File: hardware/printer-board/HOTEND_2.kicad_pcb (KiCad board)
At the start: 2 copper layers, 7 parts, among them J25 HOT_END, Q4 WSK220N04

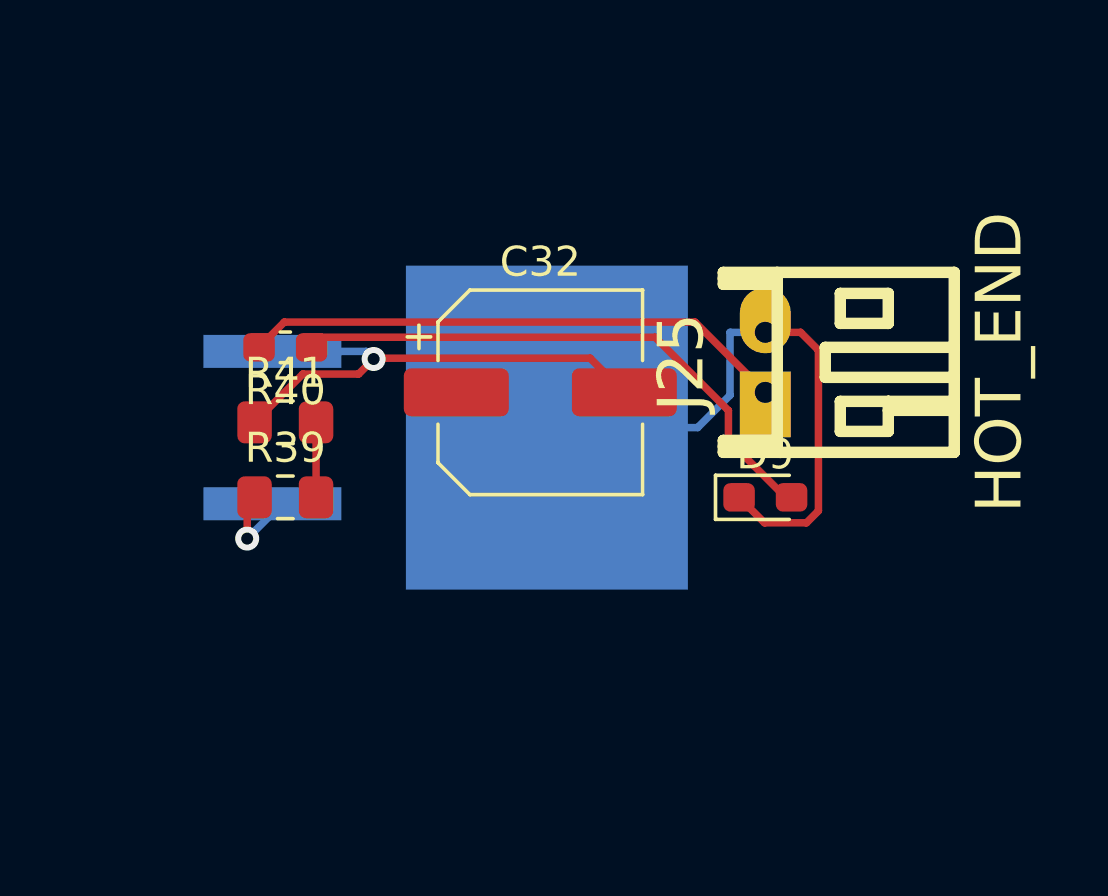
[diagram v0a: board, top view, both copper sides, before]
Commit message: update hotend,
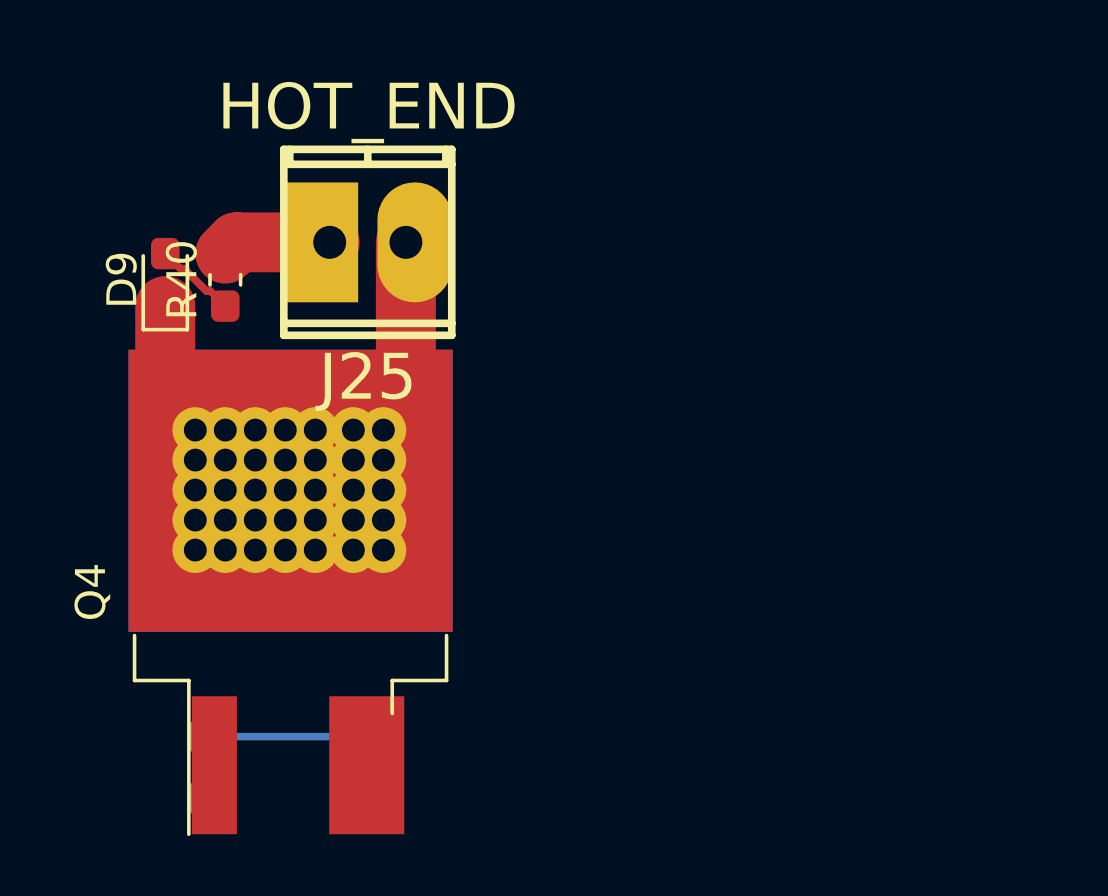
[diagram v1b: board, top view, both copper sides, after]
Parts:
- removed C32: CP100uf,16V, Capacitor_SMD:CP_Elec_6.3x5.3
- J25: footprint footprint-lib:s2b-ph-kl,hotend_output -> footprint-lib:mpt_0,5%2f2-2,54,heatbed
- Q4: footprint Package_TO_SOT_SMD:TO-263-2 -> footprint-lib:TO-263-2,drill_array; moved to F.Cu
- R39, R41: moved to B.Cu
- moved D9 21.3 mm to (4.00, 8.25), turned to 90 degrees
- moved J25 13.8 mm to (10.8, 7.00), turned to 180 degrees
- moved R41 11.8 mm to (10.8, 24.5), turned to 90 degrees
- moved R39 9.34 mm to (5.50, 24.5), turned to 90 degrees
- moved Q4 7.53 mm to (8.18, 18.7), turned to 90 degrees
- moved R40 3.01 mm to (6.00, 8.25), turned to 90 degrees
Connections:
- net Net-(D9-Pad1) renamed /-12V
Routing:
- net GND: track 17.2 -> 0.00 mm, vias 1 -> 0
- net Net-(D9-Pad2): track 18.9 -> 2.72 mm
- net +12V: track 18.2 -> 3.64 mm
- net Net-(Q4-Pad1): track 2.98 -> 0.00 mm, vias 1 -> 0
- net /HOTEND_EN: track 2.50 -> 5.25 mm
- net /-12V: track 20.4 -> 18.1 mm
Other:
- net class +12V_HC added: clearance 0.2, trace_width 2, via_dia 0.8, via_drill 0.4
- net class GND added: clearance 0.2, trace_width 2, via_dia 0.8, via_drill 0.4

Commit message: update for stepper Z,
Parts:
- added C1: CP100uf,35V, Capacitor_SMD:C_0603_1608Metric_Pad1.05x0.95mm_HandSolder, F.Cu at (190.6, 45.3)
- added C10: CP100uf,25V, Capacitor_SMD:CP_Elec_6.3x7.7, F.Cu at (297.3, 53.2)
- added C11: C104,0603, Capacitor_SMD:C_0603_1608Metric_Pad1.05x0.95mm_HandSolder, F.Cu at (297.6, 59.1)
- added C12: CP100uf,25V, Capacitor_SMD:CP_Elec_6.3x7.7, F.Cu at (240.3, 109.1)
- added C13: C104,0603, Capacitor_SMD:C_0603_1608Metric_Pad1.05x0.95mm_HandSolder, F.Cu at (237.3, 115.0)
- added C14: C106,0603, Capacitor_SMD:C_0603_1608Metric_Pad1.05x0.95mm_HandSolder, F.Cu at (295.6, 127.7)
- added C15: C106,0603, Capacitor_SMD:C_0603_1608Metric_Pad1.05x0.95mm_HandSolder, F.Cu at (292.3, 136.8)
- added C16: C106,0603, Capacitor_SMD:C_0603_1608Metric_Pad1.05x0.95mm_HandSolder, F.Cu at (292.3, 127.7)
- added C17: C106,0603, Capacitor_SMD:C_0603_1608Metric_Pad1.05x0.95mm_HandSolder, F.Cu at (295.6, 129.2)
- added C18: C106,0603, Capacitor_SMD:C_0603_1608Metric_Pad1.05x0.95mm_HandSolder, F.Cu at (292.3, 132.3)
- added C19: C104,0603, Capacitor_SMD:C_0603_1608Metric_Pad1.05x0.95mm_HandSolder, F.Cu at (221.4, 140.3)
- added C2: CP100uf,25V, Capacitor_SMD:CP_Elec_6.3x7.7, F.Cu at (160.0, 109.1)
- added C20: CP100uf,35V, Capacitor_SMD:CP_Elec_6.3x7.7, F.Cu at (235.1, 137.6)
- added C21: C104,0603, Capacitor_SMD:C_0603_1608Metric_Pad1.05x0.95mm_HandSolder, F.Cu at (295.3, 86.0)
- added C22: C10pf,0603, Capacitor_SMD:C_0603_1608Metric_Pad1.05x0.95mm_HandSolder, F.Cu at (281.9, 85.8)
- added C23: C104,0603, Capacitor_SMD:C_0603_1608Metric_Pad1.05x0.95mm_HandSolder, F.Cu at (308.3, 76.8)
- added C24: C10pf,0603, Capacitor_SMD:C_0603_1608Metric_Pad1.05x0.95mm_HandSolder, F.Cu at (285.2, 85.8)
- added C25: C104,0603, Capacitor_SMD:C_0603_1608Metric_Pad1.05x0.95mm_HandSolder, F.Cu at (295.1, 82.0)
- added C26: C104,0603, Capacitor_SMD:C_0603_1608Metric_Pad1.05x0.95mm_HandSolder, F.Cu at (295.1, 80.4)
- added C27: C104,0603, Capacitor_SMD:C_0603_1608Metric_Pad1.05x0.95mm_HandSolder, F.Cu at (298.5, 80.4)
- added C28: C104,0603, Capacitor_SMD:C_0603_1608Metric_Pad1.05x0.95mm_HandSolder, F.Cu at (295.1, 83.5)
- added C29: C105,0603, Capacitor_SMD:C_0603_1608Metric_Pad1.05x0.95mm_HandSolder, F.Cu at (305.0, 75.3)
- added C3: C104,0603, Capacitor_SMD:C_0603_1608Metric_Pad1.05x0.95mm_HandSolder, F.Cu at (166.4, 109.9)
- added C30: C104,0603, Capacitor_SMD:C_0603_1608Metric_Pad1.05x0.95mm_HandSolder, F.Cu at (298.5, 78.9)
- added C31: C104,0603, Capacitor_SMD:C_0603_1608Metric_Pad1.05x0.95mm_HandSolder, F.Cu at (291.9, 85.8)
- added C32: C104,0603, Capacitor_SMD:C_0603_1608Metric_Pad1.05x0.95mm_HandSolder, F.Cu at (288.6, 85.8)
- added C33: CP220uf,16V, Capacitor_SMD:C_0603_1608Metric_Pad1.05x0.95mm_HandSolder, F.Cu at (147.7, 149.0)
- added C34: CP220uf,16V, Capacitor_SMD:C_0603_1608Metric_Pad1.05x0.95mm_HandSolder, F.Cu at (144.3, 149.0)
- added C35: CP220uf,25V, Capacitor_SMD:C_0603_1608Metric_Pad1.05x0.95mm_HandSolder, F.Cu at (144.3, 150.5)
- added C36: CP100uf,16V, Capacitor_SMD:CP_Elec_6.3x5.3, F.Cu at (259.2, 130.5)
- added C37: CP100uf,16V, Capacitor_SMD:CP_Elec_6.3x5.3, F.Cu at (321.8, 48.1)
- added C38: CP100uf,16V, Capacitor_SMD:CP_Elec_6.3x5.3, F.Cu at (259.2, 145.1)
- added C39: CP100uf,25V, Capacitor_SMD:CP_Elec_6.3x7.7, F.Cu at (257.2, 77.0)
- added C4: CP100uf,25V, Capacitor_SMD:CP_Elec_6.3x7.7, F.Cu at (200.2, 109.1)
- added C40: C104,0603, Capacitor_SMD:C_0603_1608Metric_Pad1.05x0.95mm_HandSolder, F.Cu at (254.2, 84.5)
- added C41: CP100uf,25V, Capacitor_SMD:CP_Elec_6.3x7.7, F.Cu at (257.2, 53.2)
- added C42: C104,0603, Capacitor_SMD:C_0603_1608Metric_Pad1.05x0.95mm_HandSolder, F.Cu at (263.6, 54.0)
- added C43: C104,0603, Capacitor_SMD:C_0603_1608Metric_Pad1.05x0.95mm_HandSolder, F.Cu at (274.0, 103.0)
- added C44: CP100uf,16V, Capacitor_SMD:CP_Elec_6.3x5.3, F.Cu at (280.3, 95.8)
- added C45: C106,0603, Capacitor_SMD:C_0603_1608Metric_Pad1.05x0.95mm_HandSolder, F.Cu at (318.6, 92.3)
- added C46: C104,0603, Capacitor_SMD:C_0603_1608Metric_Pad1.05x0.95mm_HandSolder, F.Cu at (325.3, 92.3)
- added C47: C332,0603, Capacitor_SMD:C_0603_1608Metric_Pad1.05x0.95mm_HandSolder, F.Cu at (322.0, 92.3)
- added C48: C103,0603, Capacitor_SMD:C_0603_1608Metric_Pad1.05x0.95mm_HandSolder, F.Cu at (318.6, 93.8)
- added C49: C226,6.3v,0603, Capacitor_SMD:C_0603_1608Metric_Pad1.05x0.95mm_HandSolder, F.Cu at (328.7, 93.8)
- added C5: C104,0603, Capacitor_SMD:C_0603_1608Metric_Pad1.05x0.95mm_HandSolder, F.Cu at (197.2, 116.6)
- added C50: C106,0603, Capacitor_SMD:C_0603_1608Metric_Pad1.05x0.95mm_HandSolder, F.Cu at (224.8, 152.9)
- added C51: C104,0603, Capacitor_SMD:C_0603_1608Metric_Pad1.05x0.95mm_HandSolder, F.Cu at (228.1, 151.4)
- added C52: C332,0603, Capacitor_SMD:C_0603_1608Metric_Pad1.05x0.95mm_HandSolder, F.Cu at (221.4, 152.9)
- added C53: C103,0603, Capacitor_SMD:C_0603_1608Metric_Pad1.05x0.95mm_HandSolder, F.Cu at (224.8, 151.4)
- added C54: C226,6.3v,0603, Capacitor_SMD:C_0603_1608Metric_Pad1.05x0.95mm_HandSolder, F.Cu at (221.4, 151.4)
- added C6: CP100uf,25V, Capacitor_SMD:CP_Elec_6.3x7.7, F.Cu at (160.0, 133.1)
- added C7: C104,0603, Capacitor_SMD:C_0603_1608Metric_Pad1.05x0.95mm_HandSolder, F.Cu at (160.3, 139.0)
- added C8: CP100uf,25V, Capacitor_SMD:CP_Elec_6.3x7.7, F.Cu at (200.1, 133.1)
- added C9: C104,0603, Capacitor_SMD:C_0603_1608Metric_Pad1.05x0.95mm_HandSolder, F.Cu at (197.1, 140.5)
- added D1: 5V HEALTHY, LED_SMD:LED_0603_1608Metric_Pad1.05x0.95mm_HandSolder, F.Cu at (141.2, 93.6)
- added D10: LED_BLUE,0603, LED_SMD:LED_0603_1608Metric_Pad1.05x0.95mm_HandSolder, F.Cu at (315.2, 79.3)
- added D11: LED_BLUE,0603, LED_SMD:LED_0603_1608Metric_Pad1.05x0.95mm_HandSolder, F.Cu at (318.6, 79.3)
- added D12: LED_BLUE,0603, LED_SMD:LED_0603_1608Metric_Pad1.05x0.95mm_HandSolder, F.Cu at (318.6, 80.9)
- added D13: LED_BLUE,0603, LED_SMD:LED_0603_1608Metric_Pad1.05x0.95mm_HandSolder, F.Cu at (325.4, 79.3)
- added D14: LED_BLUE,0603, LED_SMD:LED_0603_1608Metric_Pad1.05x0.95mm_HandSolder, F.Cu at (322.0, 79.3)
- added D15: SD_M4, Diode_SMD:D_SOD-323_HandSoldering, F.Cu at (221.8, 136.1)
- added D16: SD_M4, Diode_SMD:D_SOD-323_HandSoldering, F.Cu at (225.8, 136.1)
- added D17: PB9, LED_SMD:LED_0603_1608Metric_Pad1.05x0.95mm_HandSolder, F.Cu at (278.5, 85.8)
- added D18: LED_RED,0603, LED_SMD:LED_0603_1608Metric_Pad1.05x0.95mm_HandSolder, F.Cu at (295.3, 102.5)
- added D19: LED_RED,0603, LED_SMD:LED_0603_1608Metric_Pad1.05x0.95mm_HandSolder, F.Cu at (265.4, 122.5)
- added D2: LED_BLUE,0603, LED_SMD:LED_0603_1608Metric_Pad1.05x0.95mm_HandSolder, F.Cu at (157.0, 115.4)
- added D20: LED_BLUE,0603, LED_SMD:LED_0603_1608Metric_Pad1.05x0.95mm_HandSolder, F.Cu at (259.8, 134.9)
- added D21: LED_BLUE,0603, LED_SMD:LED_0603_1608Metric_Pad1.05x0.95mm_HandSolder, F.Cu at (322.4, 52.4)
- added D22: LED_BLUE,0603, LED_SMD:LED_0603_1608Metric_Pad1.05x0.95mm_HandSolder, F.Cu at (272.1, 142.3)
- added D23: LED_BLUE,0603, LED_SMD:LED_0603_1608Metric_Pad1.05x0.95mm_HandSolder, F.Cu at (254.2, 81.4)
- added D24: LED_BLUE,0603, LED_SMD:LED_0603_1608Metric_Pad1.05x0.95mm_HandSolder, F.Cu at (254.2, 57.5)
- added D3: LED_BLUE,0603, LED_SMD:LED_0603_1608Metric_Pad1.05x0.95mm_HandSolder, F.Cu at (197.2, 113.5)
- added D4: LED_BLUE,0603, LED_SMD:LED_0603_1608Metric_Pad1.05x0.95mm_HandSolder, F.Cu at (157.0, 137.4)
- added D5: LED_BLUE,0603, LED_SMD:LED_0603_1608Metric_Pad1.05x0.95mm_HandSolder, F.Cu at (197.1, 137.4)
- added D6: LED_BLUE,0603, LED_SMD:LED_0603_1608Metric_Pad1.05x0.95mm_HandSolder, F.Cu at (294.3, 57.5)
- added D7: LED_BLUE,0603, LED_SMD:LED_0603_1608Metric_Pad1.05x0.95mm_HandSolder, F.Cu at (237.3, 113.5)
- added D8: LED_RED,0603, LED_SMD:LED_0603_1608Metric_Pad1.05x0.95mm_HandSolder, F.Cu at (295.3, 119.1)
- added F1: 16V/30A, w_misc_comp:fuse_smf, F.Cu at (225.0, 127.0)
- added F2: 30V/5A, w_misc_comp:fuse_smf, F.Cu at (225.0, 132.4)
- added H1: MOUNT_M3, MountingHole:MountingHole_2.7mm_M2.5, F.Cu at (3.00, 3.00)
- added H2: MOUNT_M3, MountingHole:MountingHole_2.7mm_M2.5, F.Cu at (97.0, 3.00)
- added H3: MOUNT_M3, MountingHole:MountingHole_2.7mm_M2.5, F.Cu at (3.00, 97.0)
- added H4: MOUNT_M3, MountingHole:MountingHole_2.7mm_M2.5, F.Cu at (97.0, 97.0)
- added J1: USB_DEBUG, Connector_PinHeader_1.27mm:PinHeader_1x05_P1.27mm_Vertical, F.Cu at (187.4, 45.7)
- added J10: MS_SELECT, Connector_PinHeader_2.54mm:PinHeader_2x03_P2.54mm_Vertical, F.Cu at (304.8, 46.3)
- added J11: E0, footprint-lib:b4b-ph-kl,stepper_terminal, F.Cu at (297.8, 46.6)
- added J12: MS_SELECT, Connector_PinHeader_2.54mm:PinHeader_2x03_P2.54mm_Vertical, F.Cu at (247.8, 102.3)
- added J13: E1, footprint-lib:b4b-ph-kl,stepper_terminal, F.Cu at (240.8, 102.6)
- added J14: HEATBED, footprint-lib:mpt_0,5%2f2-2,54,heatbed, F.Cu at (309.5, 113.4)
- added J15: X_MIN, footprint-lib:b3b-ph-kl,end_stop, F.Cu at (317.7, 70.5)
- added J16: X_MAX, footprint-lib:b3b-ph-kl,end_stop, F.Cu at (317.7, 75.6)
- added J17: Y_MIN, footprint-lib:b3b-ph-kl,end_stop, F.Cu at (326.1, 70.5)
- added J18: Y_MAX, footprint-lib:b3b-ph-kl,end_stop, F.Cu at (326.1, 75.6)
- added J19: Z_MIN, footprint-lib:b3b-ph-kl,end_stop, F.Cu at (334.5, 70.5)
- added J2: MS_SELECT, Connector_PinHeader_2.54mm:PinHeader_2x03_P2.54mm_Vertical, F.Cu at (167.5, 102.3)
- added J20: Z_MAX, footprint-lib:b3b-ph-kl,end_stop, F.Cu at (334.5, 75.6)
- added J21: HEATBED_TEMP, w_conn_jst-ph:b2b-ph-kl, F.Cu at (281.1, 134.1)
- added J22: HOTEND_TEMP0, w_conn_jst-ph:b2b-ph-kl, F.Cu at (281.1, 129.1)
- added J23: HOTEND_TEMP1, w_conn_jst-ph:b2b-ph-kl, F.Cu at (287.4, 129.1)
- added J24: AUX_TEMP, w_conn_jst-ph:b2b-ph-kl, F.Cu at (287.4, 134.1)
- added J26: 12V_INPUT, footprint-lib:mpt_0,5%2f2-2,54,12V_SRC, F.Cu at (239.3, 130.8)
- added J27: 12V_OUT, footprint-lib:mpt_0,5%2f2-2,54,12V_SRC, F.Cu at (233.3, 130.8)
- added J28: SWD, Connector_PinHeader_1.27mm:PinHeader_1x04_P1.27mm_Vertical, F.Cu at (307.2, 69.6)
- added J29: USB_DEBUG, Connector_PinHeader_1.27mm:PinHeader_1x05_P1.27mm_Vertical, F.Cu at (157.4, 149.5)
- added J3: X, footprint-lib:b4b-ph-kl,stepper_terminal, F.Cu at (160.5, 102.6)
- added J30: PWR_DEBUG, Connector_PinHeader_1.27mm:PinHeader_1x05_P1.27mm_Vertical, F.Cu at (141.1, 149.5)
- added J31: HOT_END, footprint-lib:mpt_0,5%2f2-2,54,heatbed, F.Cu at (309.5, 96.8)
- added J32: HOT_END, footprint-lib:mpt_0,5%2f2-2,54,heatbed, F.Cu at (279.6, 116.8)
- added J33: TO FAN0, footprint-lib:b2b-ph-kl,fan_pwm_out, F.Cu at (267.2, 129.1)
- added J34: TO FAN1, footprint-lib:b2b-ph-kl,fan_pwm_out, F.Cu at (329.8, 46.6)
- added J35: TO FAN2, footprint-lib:b2b-ph-kl,fan_pwm_out, F.Cu at (267.2, 143.6)
- added J36: MS_SELECT, Connector_PinHeader_2.54mm:PinHeader_2x03_P2.54mm_Vertical, F.Cu at (264.7, 70.2)
- added J37: Z2, footprint-lib:b4b-ph-kl,stepper_terminal, F.Cu at (257.7, 70.5)
- added J38: MS_SELECT, Connector_PinHeader_2.54mm:PinHeader_2x03_P2.54mm_Vertical, F.Cu at (264.7, 46.3)
- added J39: Y, footprint-lib:b4b-ph-kl,stepper_terminal, F.Cu at (257.7, 46.6)
- added J4: MS_SELECT, Connector_PinHeader_2.54mm:PinHeader_2x03_P2.54mm_Vertical, F.Cu at (207.7, 102.3)
- added J40: Conn_01x07, Connector_PinHeader_1.27mm:PinHeader_1x07_P1.27mm_Vertical, F.Cu at (273.9, 93.4)
- added J41: EXP1, Connector_PinHeader_2.54mm:PinHeader_2x05_P2.54mm_Vertical, F.Cu at (261.8, 94.1)
- added J42: EXP2, Connector_PinHeader_2.54mm:PinHeader_2x05_P2.54mm_Vertical, F.Cu at (268.0, 94.1)
- added J5: Z, footprint-lib:b4b-ph-kl,stepper_terminal, F.Cu at (200.7, 102.6)
- added J6: MS_SELECT, Connector_PinHeader_2.54mm:PinHeader_2x03_P2.54mm_Vertical, F.Cu at (167.5, 126.2)
- added J7: Z1, footprint-lib:b4b-ph-kl,stepper_terminal, F.Cu at (160.5, 126.5)
- added J8: MS_SELECT, Connector_PinHeader_2.54mm:PinHeader_2x03_P2.54mm_Vertical, F.Cu at (207.6, 126.2)
- added J9: Z3, footprint-lib:b4b-ph-kl,stepper_terminal, F.Cu at (200.6, 126.5)
- added JP1: Jumper_NO_Small, Jumper:SolderJumper-2_P1.3mm_Open_TrianglePad1.0x1.5mm, F.Cu at (141.2, 95.7)
- added JP2: Jumper_NO_Small, Jumper:SolderJumper-2_P1.3mm_Open_TrianglePad1.0x1.5mm, F.Cu at (187.5, 54.7)
- added JP3: Jumper_NO_Small, Jumper:SolderJumper-2_P1.3mm_Open_TrianglePad1.0x1.5mm, F.Cu at (194.0, 45.8)
- added JP4: Jumper_NO_Small, Jumper:SolderJumper-2_P1.3mm_Open_TrianglePad1.0x1.5mm, F.Cu at (144.6, 94.1)
- added JP5: Jumper_NO_Small, SolderJumper-2_P1.3mm_Open_TrianglePad1.0x1.5mm, F.Cu at (221.4, 138.3)
- added JP6: Jumper_NO_Small, SolderJumper-2_P1.3mm_Open_TrianglePad1.0x1.5mm, F.Cu at (298.5, 84.0)
- added JP7: Jumper_NO_Small, SolderJumper-2_P1.3mm_Open_TrianglePad1.0x1.5mm, F.Cu at (305.2, 78.8)
- added L1: L_Small, w_smd_inductors:inductor_smd_0603, F.Cu at (301.3, 83.4)
- added L2: L_15uH, w_smd_inductors:inductor_smd_4.8x2.8mm, F.Cu at (327.2, 88.8)
- added L3: L_15uH, w_smd_inductors:inductor_smd_4.8x2.8mm, F.Cu at (229.9, 147.9)
- added Q1: WSK220N04, footprint-lib:TO-263-2,drill_array, F.Cu at (298.1, 112.6)
- added Q2: STP55NF06, footprint-lib:TO-263-2,drill_array, F.Cu at (298.1, 96.0)
- added Q3: STP55NF06, footprint-lib:TO-263-2,drill_array, F.Cu at (268.3, 116.0)
- added Q5: D882, footprint-lib:SOT-89-3,thermal_vias, F.Cu at (329.1, 52.2)
- added Q6: D882, footprint-lib:SOT-89-3,thermal_vias, F.Cu at (266.5, 149.2)
- added R1: R153,0603, Resistor_SMD:R_0603_1608Metric_Pad1.05x0.95mm_HandSolder, F.Cu at (238.4, 94.5)
- added R10: R103,0603, Resistor_SMD:R_0603_1608Metric_Pad1.05x0.95mm_HandSolder, F.Cu at (160.4, 115.4)
- added R11: R104,0603, Resistor_SMD:R_0603_1608Metric_Pad1.05x0.95mm_HandSolder, F.Cu at (197.2, 115.0)
- added R12: R102,0603, Resistor_SMD:R_0603_1608Metric_Pad1.05x0.95mm_HandSolder, F.Cu at (206.6, 109.9)
- added R13: R103,0603, Resistor_SMD:R_0603_1608Metric_Pad1.05x0.95mm_HandSolder, F.Cu at (200.5, 115.0)
- added R14: R104,0603, Resistor_SMD:R_0603_1608Metric_Pad1.05x0.95mm_HandSolder, F.Cu at (166.4, 133.9)
- added R15: R102,0603, Resistor_SMD:R_0603_1608Metric_Pad1.05x0.95mm_HandSolder, F.Cu at (157.0, 139.0)
- added R16: R103,0603, Resistor_SMD:R_0603_1608Metric_Pad1.05x0.95mm_HandSolder, F.Cu at (157.0, 140.5)
- added R17: R104,0603, Resistor_SMD:R_0603_1608Metric_Pad1.05x0.95mm_HandSolder, F.Cu at (197.1, 139.0)
- added R18: R102,0603, Resistor_SMD:R_0603_1608Metric_Pad1.05x0.95mm_HandSolder, F.Cu at (206.5, 133.9)
- added R19: R103,0603, Resistor_SMD:R_0603_1608Metric_Pad1.05x0.95mm_HandSolder, F.Cu at (200.4, 139.0)
- added R2: R153,0603, Resistor_SMD:R_0603_1608Metric_Pad1.05x0.95mm_HandSolder, F.Cu at (238.4, 93.0)
- added R20: R104,0603, Resistor_SMD:R_0603_1608Metric_Pad1.05x0.95mm_HandSolder, F.Cu at (303.7, 54.0)
- added R21: R102,0603, Resistor_SMD:R_0603_1608Metric_Pad1.05x0.95mm_HandSolder, F.Cu at (294.3, 60.6)
- added R22: R103,0603, Resistor_SMD:R_0603_1608Metric_Pad1.05x0.95mm_HandSolder, F.Cu at (294.3, 59.1)
- added R23: R104,0603, Resistor_SMD:R_0603_1608Metric_Pad1.05x0.95mm_HandSolder, F.Cu at (240.6, 115.0)
- added R24: R102,0603, Resistor_SMD:R_0603_1608Metric_Pad1.05x0.95mm_HandSolder, F.Cu at (246.7, 109.9)
- added R25: R103,0603, Resistor_SMD:R_0603_1608Metric_Pad1.05x0.95mm_HandSolder, F.Cu at (237.3, 116.6)
- added R26: R100,0805, Resistor_SMD:R_0805_2012Metric_Pad1.15x1.40mm_HandSolder, F.Cu at (308.3, 117.6)
- added R27: R104,0805, Resistor_SMD:R_0805_2012Metric_Pad1.15x1.40mm_HandSolder, F.Cu at (291.7, 119.3)
- added R28: R182,0603, Resistor_SMD:R_0603_1608Metric_Pad1.05x0.95mm_HandSolder, F.Cu at (298.6, 119.0)
- added R29: R102,0603, Resistor_SMD:R_0603_1608Metric_Pad1.05x0.95mm_HandSolder, F.Cu at (332.0, 82.3)
- added R3: R152,0603, Resistor_SMD:R_0603_1608Metric_Pad1.05x0.95mm_HandSolder, F.Cu at (241.7, 93.0)
- added R30: R102,0603, Resistor_SMD:R_0603_1608Metric_Pad1.05x0.95mm_HandSolder, F.Cu at (328.7, 79.3)
- added R31: R102,0603, Resistor_SMD:R_0603_1608Metric_Pad1.05x0.95mm_HandSolder, F.Cu at (325.3, 80.9)
- added R32: R102,0603, Resistor_SMD:R_0603_1608Metric_Pad1.05x0.95mm_HandSolder, F.Cu at (328.7, 80.8)
- added R33: R102,0603, Resistor_SMD:R_0603_1608Metric_Pad1.05x0.95mm_HandSolder, F.Cu at (328.7, 82.3)
- added R34: R102,0603, Resistor_SMD:R_0603_1608Metric_Pad1.05x0.95mm_HandSolder, F.Cu at (322.0, 80.9)
- added R35: R472,0603, Resistor_SMD:R_0603_1608Metric_Pad1.05x0.95mm_HandSolder, F.Cu at (292.3, 129.2)
- added R36: R472,0603, Resistor_SMD:R_0603_1608Metric_Pad1.05x0.95mm_HandSolder, F.Cu at (292.3, 130.7)
- added R37: R472,0603, Resistor_SMD:R_0603_1608Metric_Pad1.05x0.95mm_HandSolder, F.Cu at (292.3, 135.3)
- added R38: R472,0603, Resistor_SMD:R_0603_1608Metric_Pad1.05x0.95mm_HandSolder, F.Cu at (295.6, 132.3)
- added R4: R220,0603, Resistor_SMD:R_0603_1608Metric_Pad1.05x0.95mm_HandSolder, F.Cu at (187.5, 52.7)
- added R42: R0,0603, Resistor_SMD:R_0603_1608Metric_Pad1.05x0.95mm_HandSolder, F.Cu at (308.3, 75.3)
- added R43: R0,0603, Resistor_SMD:R_0603_1608Metric_Pad1.05x0.95mm_HandSolder, F.Cu at (295.1, 78.9)
- added R44: R102,0603, Resistor_SMD:R_0603_1608Metric_Pad1.05x0.95mm_HandSolder, F.Cu at (301.8, 78.9)
- added R45: R103,0603, Resistor_SMD:R_0603_1608Metric_Pad1.05x0.95mm_HandSolder, F.Cu at (305.0, 76.8)
- added R46: R103,0603, Resistor_SMD:R_0603_1608Metric_Pad1.05x0.95mm_HandSolder, F.Cu at (298.5, 82.0)
- added R47: R220,0603, Resistor_SMD:R_0603_1608Metric_Pad1.05x0.95mm_HandSolder, F.Cu at (160.7, 150.5)
- added R48: R220,0603, Resistor_SMD:R_0603_1608Metric_Pad1.05x0.95mm_HandSolder, F.Cu at (164.0, 149.0)
- added R49: R152,0603, Resistor_SMD:R_0603_1608Metric_Pad1.05x0.95mm_HandSolder, F.Cu at (160.7, 149.0)
- added R5: R220,0603, Resistor_SMD:R_0603_1608Metric_Pad1.05x0.95mm_HandSolder, F.Cu at (147.9, 93.6)
- added R50: R100,0805, Resistor_SMD:R_0805_2012Metric_Pad1.15x1.40mm_HandSolder, F.Cu at (308.3, 101.0)
- added R51: R104,0805, Resistor_SMD:R_0805_2012Metric_Pad1.15x1.40mm_HandSolder, F.Cu at (291.7, 102.7)
- added R52: R182,0603, Resistor_SMD:R_0603_1608Metric_Pad1.05x0.95mm_HandSolder, F.Cu at (298.6, 102.4)
- added R53: R100,0805, Resistor_SMD:R_0805_2012Metric_Pad1.15x1.40mm_HandSolder, F.Cu at (261.8, 122.7)
- added R54: R104,0805, Resistor_SMD:R_0805_2012Metric_Pad1.15x1.40mm_HandSolder, F.Cu at (278.5, 121.0)
- added R55: R182,0603, Resistor_SMD:R_0603_1608Metric_Pad1.05x0.95mm_HandSolder, F.Cu at (268.8, 122.5)
- added R56: R100,0805, Resistor_SMD:R_0805_2012Metric_Pad1.15x1.40mm_HandSolder, F.Cu at (272.3, 127.9)
- added R57: R104,0805, Resistor_SMD:R_0805_2012Metric_Pad1.15x1.40mm_HandSolder, F.Cu at (256.2, 135.1)
- added R58: R100,0603, Resistor_SMD:R_0603_1608Metric_Pad1.05x0.95mm_HandSolder, F.Cu at (259.4, 136.8)
- added R59: R182,0603, Resistor_SMD:R_0603_1608Metric_Pad1.05x0.95mm_HandSolder, F.Cu at (256.0, 136.8)
- added R6: R152,0603, Resistor_SMD:R_0603_1608Metric_Pad1.05x0.95mm_HandSolder, F.Cu at (190.6, 48.3)
- added R60: R100,0805, Resistor_SMD:R_0805_2012Metric_Pad1.15x1.40mm_HandSolder, F.Cu at (334.8, 45.5)
- added R61: R104,0805, Resistor_SMD:R_0805_2012Metric_Pad1.15x1.40mm_HandSolder, F.Cu at (318.8, 52.6)
- added R62: R100,0603, Resistor_SMD:R_0603_1608Metric_Pad1.05x0.95mm_HandSolder, F.Cu at (318.6, 54.4)
- added R63: R182,0603, Resistor_SMD:R_0603_1608Metric_Pad1.05x0.95mm_HandSolder, F.Cu at (322.0, 54.4)
- added R64: R100,0805, Resistor_SMD:R_0603_1608Metric_Pad1.05x0.95mm_HandSolder, F.Cu at (259.8, 149.4)
- added R65: R104,0805, Resistor_SMD:R_0805_2012Metric_Pad1.15x1.40mm_HandSolder, F.Cu at (256.2, 149.6)
- added R66: R100,0603, Resistor_SMD:R_0603_1608Metric_Pad1.05x0.95mm_HandSolder, F.Cu at (256.0, 151.4)
- added R67: R182,0603, Resistor_SMD:R_0603_1608Metric_Pad1.05x0.95mm_HandSolder, F.Cu at (259.4, 151.4)
- added R68: R104,0603, Resistor_SMD:R_0603_1608Metric_Pad1.05x0.95mm_HandSolder, F.Cu at (257.5, 83.0)
- added R69: R102,0603, Resistor_SMD:R_0603_1608Metric_Pad1.05x0.95mm_HandSolder, F.Cu at (254.2, 83.0)
- added R7: R102,0603, Resistor_SMD:R_0603_1608Metric_Pad1.05x0.95mm_HandSolder, F.Cu at (190.6, 46.8)
- added R70: R103,0603, Resistor_SMD:R_0603_1608Metric_Pad1.05x0.95mm_HandSolder, F.Cu at (263.6, 77.8)
- added R71: R104,0603, Resistor_SMD:R_0603_1608Metric_Pad1.05x0.95mm_HandSolder, F.Cu at (257.5, 59.1)
- added R72: R102,0603, Resistor_SMD:R_0603_1608Metric_Pad1.05x0.95mm_HandSolder, F.Cu at (254.2, 60.6)
- added R73: R103,0603, Resistor_SMD:R_0603_1608Metric_Pad1.05x0.95mm_HandSolder, F.Cu at (254.2, 59.1)
- added R74: R562,0603, Resistor_SMD:R_0603_1608Metric_Pad1.05x0.95mm_HandSolder, F.Cu at (328.7, 92.3)
- added R75: R103,0603, Resistor_SMD:R_0603_1608Metric_Pad1.05x0.95mm_HandSolder, F.Cu at (325.3, 93.8)
- added R76: R333,0603, Resistor_SMD:R_0603_1608Metric_Pad1.05x0.95mm_HandSolder, F.Cu at (322.0, 93.8)
- added R77: R562,0603, Resistor_SMD:R_0603_1608Metric_Pad1.05x0.95mm_HandSolder, F.Cu at (228.1, 152.9)
- added R78: R103,0603, Resistor_SMD:R_0603_1608Metric_Pad1.05x0.95mm_HandSolder, F.Cu at (231.5, 151.4)
- added R79: R333,0603, Resistor_SMD:R_0603_1608Metric_Pad1.05x0.95mm_HandSolder, F.Cu at (231.5, 152.9)
- added R8: R104,0603, Resistor_SMD:R_0805_2012Metric_Pad1.15x1.40mm_HandSolder, F.Cu at (157.2, 113.7)
- added R9: R102,0603, Resistor_SMD:R_0603_1608Metric_Pad1.05x0.95mm_HandSolder, F.Cu at (157.0, 117.0)
- added SW1: SW_Push, Button_Switch_SMD:SW_SPST_CK_RS282G05A3, F.Cu at (298.4, 76.1)
- added TH1: Thermistor_NTC, Resistor_SMD:R_0603_1608Metric_Pad1.05x0.95mm_HandSolder, F.Cu at (295.6, 130.7)
- added U1: orange_pi_zero, footprint-lib:orangepi-zero, F.Cu at (139.8, 92.6)
- added U10: A4988_MODULE, footprint-lib:Pololu_Breakout-16_15.2x20.3mm, F.Cu at (238.2, 46.0)
- added U11: MP2303A_ALT, footprint-lib:SOIC-8_3.9x4.9mm_P1.27mm,thermal_via, F.Cu at (320.7, 88.8)
- added U12: MP2303A_ALT, footprint-lib:SOIC-8_3.9x4.9mm_P1.27mm,thermal_via, F.Cu at (223.5, 147.9)
- added U2: A4988_MODULE, footprint-lib:Pololu_Breakout-16_15.2x20.3mm, F.Cu at (141.1, 102.0)
- added U3: A4988_MODULE, footprint-lib:Pololu_Breakout-16_15.2x20.3mm, F.Cu at (181.3, 102.0)
- added U4: A4988_MODULE, footprint-lib:Pololu_Breakout-16_15.2x20.3mm, F.Cu at (141.1, 125.9)
- added U5: A4988_MODULE, footprint-lib:Pololu_Breakout-16_15.2x20.3mm, F.Cu at (181.2, 125.9)
- added U6: A4988_MODULE, footprint-lib:Pololu_Breakout-16_15.2x20.3mm, F.Cu at (278.4, 46.0)
- added U7: A4988_MODULE, footprint-lib:Pololu_Breakout-16_15.2x20.3mm, F.Cu at (221.4, 102.0)
- added U8: STM32F407VET6, w_smd_lqfp:TQFP-100, F.Cu at (285.1, 76.7)
- added U9: A4988_MODULE, footprint-lib:Pololu_Breakout-16_15.2x20.3mm, F.Cu at (238.2, 69.9)
- added Y1: O_8M, Crystal:Crystal_HC49-4H_Vertical, F.Cu at (297.1, 71.2)
- D9: value LED_RED,0603 -> LED_BLUE,0603
- J25: value HOT_END -> 12V_INPUT_2; footprint footprint-lib:mpt_0,5%2f2-2,54,heatbed -> footprint-lib:mpt_0,5%2f2-2,54,12V_SRC
- Q4: value WSK220N04 -> D882; footprint footprint-lib:TO-263-2,drill_array -> footprint-lib:SOT-89-3,thermal_vias
- R39: value R100,0805 -> R472,0603; footprint Resistor_SMD:R_0805_2012Metric_Pad1.15x1.40mm_HandSolder -> Resistor_SMD:R_0603_1608Metric_Pad1.05x0.95mm_HandSolder; moved to F.Cu
- R40: value R182,0603 -> R472,0603
- R41: value R104,0805 -> R472,0603; footprint Resistor_SMD:R_0805_2012Metric_Pad1.15x1.40mm_HandSolder -> Resistor_SMD:R_0603_1608Metric_Pad1.05x0.95mm_HandSolder; moved to F.Cu
- moved D9 319.6 mm to (315.2, 80.9), turned to 0 degrees
- moved R39 306.9 mm to (292.3, 133.8), turned to 0 degrees
- moved R40 304.9 mm to (301.8, 82.0), turned to 0 degrees
- moved R41 296.4 mm to (301.8, 80.4), turned to 0 degrees
- moved Q4 283.2 mm to (266.5, 134.6), turned to 0 degrees
- moved J25 265.2 mm to (245.3, 130.8), turned to 0 degrees
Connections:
- D9 pad 1: /-12V -> /END_STOP/X_MIN
- J25 pad 1: +12V -> Net-(F1-Pad1)
- J25 pad 2: /-12V -> GND
- Q4 pad 2: /-12V -> Net-(Q4-Pad2)
- R39 pad 1: Net-(Q4-Pad1) -> +3V3
- R39 pad 2: /HOTEND_EN -> /Thermistors/PCB_TEMP
- R40 pad 1: Net-(D9-Pad2) -> Net-(JP6-Pad1)
- R40 pad 2: +12V -> +3V3
- R41 pad 1: GND -> Net-(JP7-Pad1)
- R41 pad 2: /HOTEND_EN -> +3V3
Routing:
- net /-12V: track 18.1 -> 0.00 mm
- net /HOTEND_EN: track 5.25 -> 0.00 mm
- net +12V: track 3.64 -> 0.00 mm
- net Net-(D9-Pad2): track 2.72 -> 0.00 mm
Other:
- board outline added: 100 x 100 mm
- net class +12V_HC removed
- net class GND removed
